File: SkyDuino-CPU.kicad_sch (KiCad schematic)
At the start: 38 parts, among them J11 DBG, J12 USB-A RMT, J13 DISP, J14 USB_C Artisan, SW1 BOOT, U10 USBLC6-2SC6, U7 20MHz, U8 USBLC6-2SC6, U9 STM32F412RET6, Y1 32.768kHz

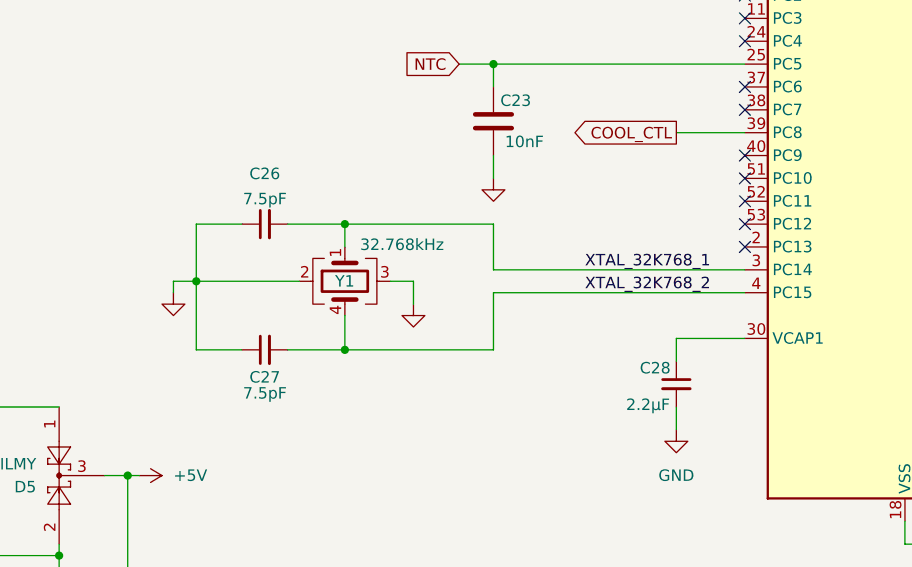
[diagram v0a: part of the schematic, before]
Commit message: Remove LSE from schematic
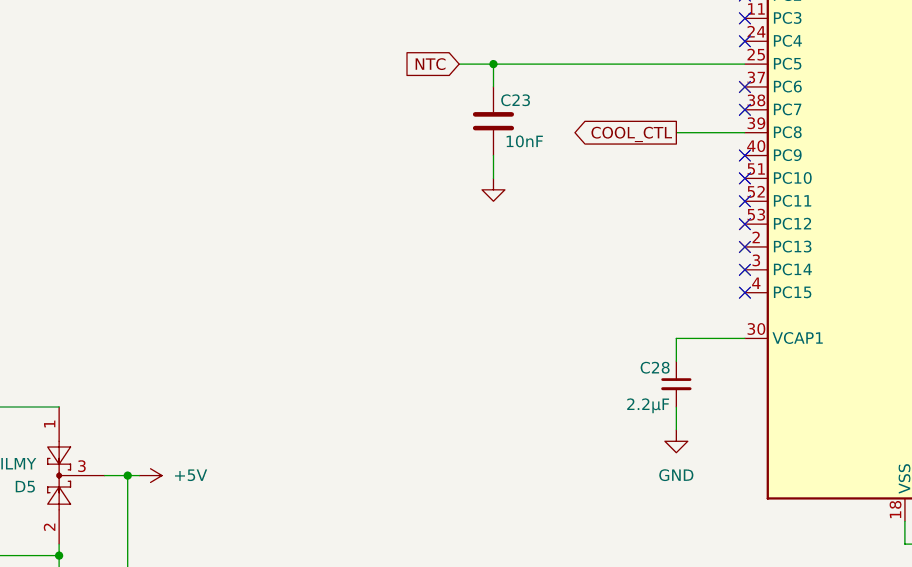
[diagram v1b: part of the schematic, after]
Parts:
- removed C26, C27: 7.5pF, Capacitor_SMD:C_0805_2012Metric_Pad1.18x1.45mm_HandSolder, symbol Device:C_Small
- removed Y1: 32.768kHz, Oscillators:Diodes Inc G43270021, symbol Device:Crystal_GND23
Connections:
- net XTAL_32K768_1: no longer names the net of U9.3 (PC14)
- net XTAL_32K768_2: no longer names the net of U9.4 (PC15)
- no-connect marks 29 -> 31

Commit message: Replace 20MHz Oscilator with JLCPCB one
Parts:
- U7: LCSC C1857136 -> C7431315; Manufacturer p/n 2520Z20.C15X -> SX2M20.000B10F20TNN; Mouser p/n 346-2520Z20.C15X -> (none)
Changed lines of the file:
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@@
 			)
 		)
-		(property "Datasheet" "https://www.mouser.com/datasheet/2/40/clock_z_x_e-3044365.pdf"
+		(property "Datasheet" "https://wmsc.lcsc.com/wmsc/upload/file/pdf/v2/lcsc/2406051011_Shenzhen-SCTF-Elec-SX2M20-000B10F20TNN_C7431315.pdf"
 			(at 96.52 58.42 0)
 			(effects
@@
 			)
 		)
-		(property "LCSC" "C1857136"
+		(property "LCSC" "C7431315"
 			(at 92.71 62.23 0)
 			(effects
@@
 			)
 		)
-		(property "Mouser p/n" "346-2520Z20.C15X"
+		(property "Mouser p/n" ""
 			(at 92.71 62.23 0)
 			(effects
@@
 			)
 		)
-		(property "Manufacturer p/n" "2520Z20.C15X"
+		(property "Manufacturer p/n" "SX2M20.000B10F20TNN"
 			(at 92.71 62.23 0)
 			(effects
+				(font
+					(size 1.27 1.27)
+				)
+				(hide yes)
+			)
+		)
+		(property "Config" ""
+			(at 92.71 62.23 0)
+			(effects
